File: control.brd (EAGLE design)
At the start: 156 x 38 mm, 68 parts, among them IC3 ATTINY85-20S, U1 L293DD013TR

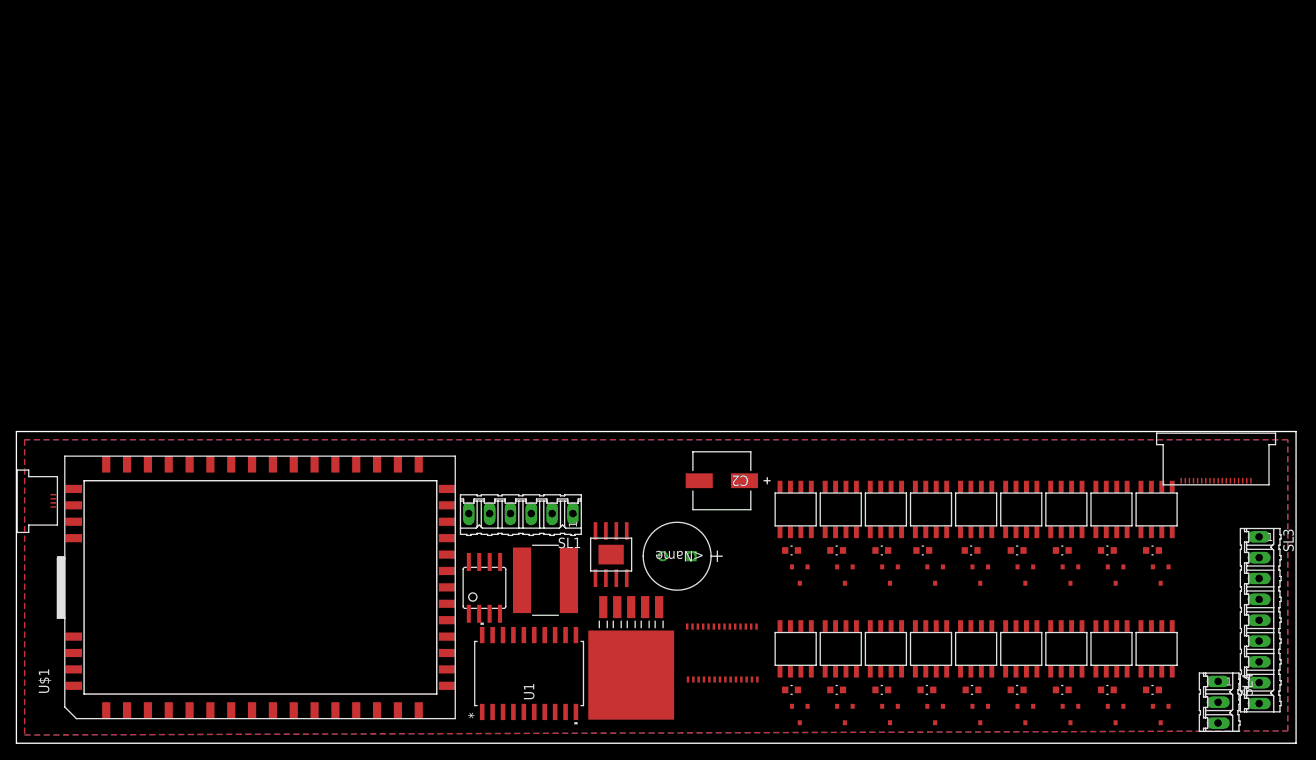
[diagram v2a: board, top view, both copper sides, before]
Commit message: setts up warm cool LED support
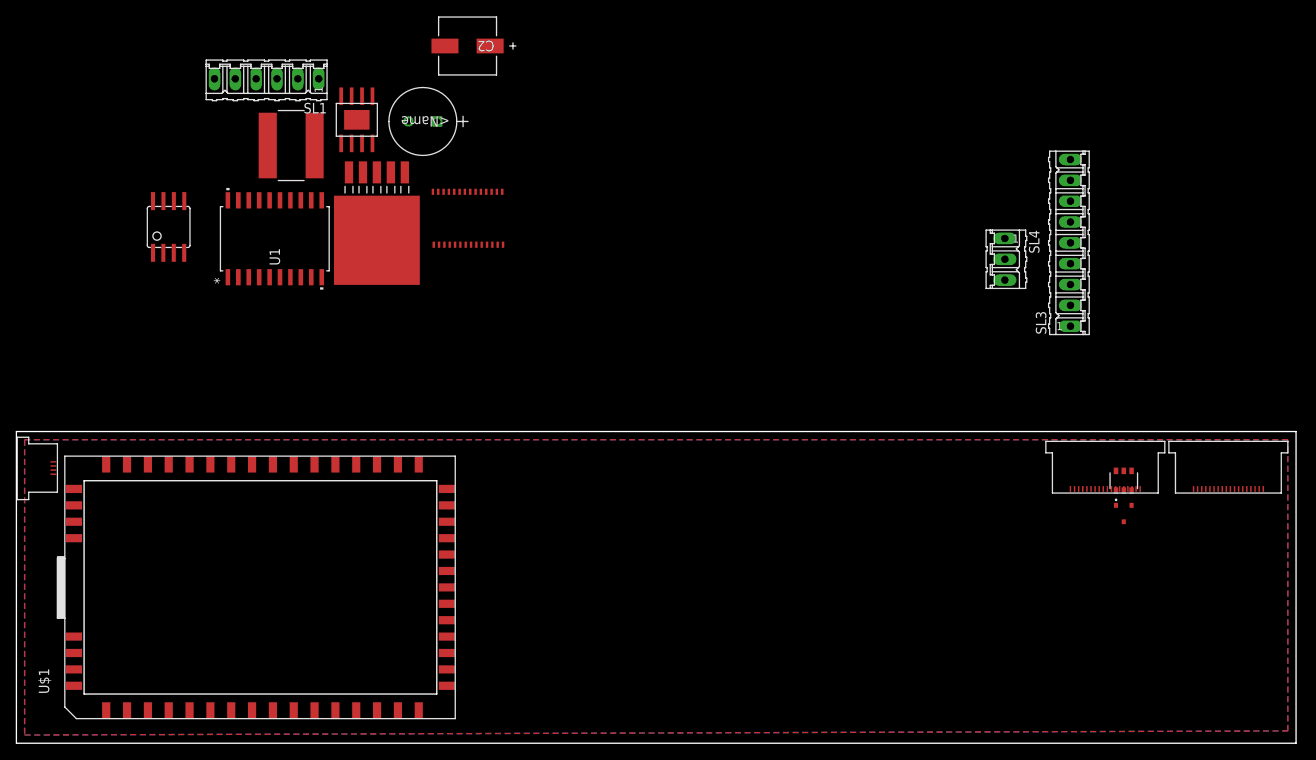
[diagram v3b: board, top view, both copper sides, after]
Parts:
- removed R1, R10, R11, R12, R13, R14, R15, R16, R17, R19, R2, R3, R4, R5, R6, R7, R8, R9: RC0603FR-0710RL, Smile_Shade:RC0603N
- removed U$10, U$12, U$14, U$16, U$18, U$20, U$22, U$24, U$26, U$28, U$30, U$32, U$34, U$4, U$41, U$6, U$8: 2N7002P, Smile_Shade:SOT23
- removed U$11, U$13, U$15, U$17, U$19, U$21, U$23, U$25, U$27, U$29, U$3, U$31, U$33, U$35, U$40, U$5, U$7, U$9: NUD4011DR2G, Smile_Shade:8SOIC
- added U$2: BCR420UW6-7, Smile_Shade:SOT26
- added U$80: SFV18R-3STBE1HLF, Smile_Shade:SFV18R-3STBE1HLF
- moved C2 61.4 mm to (55.0, 85.0)
- moved SL1 61.4 mm to (30.5, 81.0)
- moved U$36 61.4 mm to (33.5, 72.9)
- moved U$37 61.4 mm to (55.0, 64.0)
- moved U$42 61.4 mm to (41.5, 76.0)
- moved U$43 61.4 mm to (43.9, 61.3)
- moved U1 61.4 mm to (31.5, 61.5)
- moved C1 61.4 mm to (47.8, 75.8)
- moved SL4 59.9 mm to (120.5, 59.0)
- moved IC3 58.5 mm to (18.6, 62.9)
- moved SL3 51.4 mm to (128.5, 61.0), turned to 90 degrees
- moved U$38 24.9 mm to (135.0, 28.0)
- moved U$39 4.00 mm to (5.00, 36.5)
- moved U$44 1.80 mm to (152.0, 31.0)
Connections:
- removed net 48: R16.2, U$35.P$1
- removed net N$1: U$3.P$4, U$4.P$3
- removed net N$10: R4.1, U$11.P$3
- removed net N$11: U$12.P$3, U$13.P$4
- removed net N$12: R5.1, U$13.P$3
- removed net N$13: U$10.P$3, U$15.P$4
- removed net N$14: R6.1, U$15.P$3
- removed net N$15: U$17.P$4, U$38.P$3
- removed net N$16: R8.1, U$17.P$3
- removed net N$17: U$18.P$3, U$25.P$4
- removed net N$18: R7.1, U$25.P$3
- removed net N$19: U$20.P$3, U$23.P$4
- removed net N$20: R9.1, U$23.P$3
- removed net N$21: U$21.P$4, U$22.P$3
- removed net N$22: R10.1, U$21.P$3
- removed net N$23: U$19.P$4, U$24.P$3
- removed net N$24: R11.1, U$19.P$3
- removed net N$25: U$27.P$4, U$32.P$3
- removed net N$26: R15.1, U$27.P$3
- removed net N$27: U$29.P$4, U$30.P$3
- removed net N$28: R14.1, U$29.P$3
- removed net N$29: U$28.P$3, U$31.P$4
- removed net N$3: U$5.P$4, U$6.P$3
- removed net N$30: R13.1, U$31.P$3
- removed net N$31: U$26.P$3, U$33.P$4
- removed net N$32: R12.1, U$33.P$3
- removed net N$35: U$34.P$3, U$35.P$4
- removed net N$36: R16.1, U$35.P$3
- removed net N$37: U$40.P$4, U$41.P$3
- removed net N$38: R17.1, U$40.P$3
- removed net N$4: R1.1, U$5.P$3
- removed net N$5: U$7.P$4, U$8.P$3
- removed net N$6: R2.1, U$7.P$3
- removed net N$7: U$16.P$3, U$9.P$4
- removed net N$8: R3.1, U$9.P$3
- removed net N$9: U$11.P$4, U$14.P$3
- removed net ZN16: U$41.P$2
- net 48V: no longer R1.2, R10.2, R11.2, R12.2, R13.2, R14.2, R15.2, R17.2, R19.2, R2.2, R3.2, R4.2, R5.2, R6.2, R7.2, R8.2, R9.2, U$11.P$1, U$13.P$1, U$15.P$1, U$17.P$1, U$19.P$1, U$21.P$1, U$23.P$1, U$25.P$1, U$27.P$1, U$29.P$1, U$3.P$1, U$31.P$1, U$33.P$1, U$40.P$1, U$5.P$1, U$7.P$1, U$9.P$1
- net GND: now also U$2.4; no longer U$10.P$1, U$12.P$1, U$14.P$1, U$16.P$1, U$18.P$1, U$20.P$1, U$22.P$1, U$24.P$1, U$26.P$1, U$28.P$1, U$30.P$1, U$32.P$1, U$34.P$1, U$4.P$1, U$41.P$1, U$6.P$1, U$8.P$1
- net LEDSTR_1: now also U$2.2, U$2.3, U$2.5; no longer U$17.P$5, U$17.P$6, U$17.P$7, U$17.P$8
- net LEDSTR_10: no longer U$23.P$5, U$23.P$6, U$23.P$7, U$23.P$8
- net LEDSTR_11: no longer U$21.P$5, U$21.P$6, U$21.P$7, U$21.P$8
- net LEDSTR_12: no longer U$19.P$5, U$19.P$6, U$19.P$7, U$19.P$8
- net LEDSTR_13: no longer U$27.P$5, U$27.P$6, U$27.P$7, U$27.P$8
- net LEDSTR_14: no longer U$29.P$5, U$29.P$6, U$29.P$7, U$29.P$8
- net LEDSTR_15: no longer U$31.P$5, U$31.P$6, U$31.P$7, U$31.P$8
- net LEDSTR_16: no longer U$33.P$5, U$33.P$6, U$33.P$7, U$33.P$8
- net LEDSTR_17: no longer U$35.P$5, U$35.P$6, U$35.P$7, U$35.P$8
- net LEDSTR_18: no longer U$40.P$5, U$40.P$6, U$40.P$7, U$40.P$8
- net LEDSTR_2: no longer U$3.P$5, U$3.P$6, U$3.P$7, U$3.P$8
- net LEDSTR_3: no longer U$5.P$5, U$5.P$6, U$5.P$7, U$5.P$8
- net LEDSTR_4: no longer U$7.P$5, U$7.P$6, U$7.P$7, U$7.P$8
- net LEDSTR_5: no longer U$9.P$5, U$9.P$6, U$9.P$7, U$9.P$8
- net LEDSTR_6: no longer U$11.P$5, U$11.P$6, U$11.P$7, U$11.P$8
- net LEDSTR_7: no longer U$13.P$5, U$13.P$6, U$13.P$7, U$13.P$8
- net LEDSTR_8: no longer U$15.P$5, U$15.P$6, U$15.P$7, U$15.P$8
- net LEDSTR_9: no longer U$25.P$5, U$25.P$6, U$25.P$7, U$25.P$8
- net N$2: now also U$2.1, U$38.P$3; no longer R19.1, U$3.P$3
- net ZN1: no longer U$4.P$2
- net ZN10: no longer U$30.P$2
- net ZN11: no longer U$32.P$2
- net ZN12: no longer U$24.P$2
- net ZN13: no longer U$18.P$2
- net ZN14: no longer U$20.P$2
- net ZN15: no longer U$22.P$2
- net ZN2: no longer U$6.P$2
- net ZN3: no longer U$8.P$2
- net ZN4: no longer U$12.P$2
- net ZN5: no longer U$14.P$2
- net ZN6: no longer U$16.P$2
- net ZN7: no longer U$10.P$2
- net ZN8: no longer U$26.P$2, U$34.P$2
- net ZN9: no longer U$28.P$2

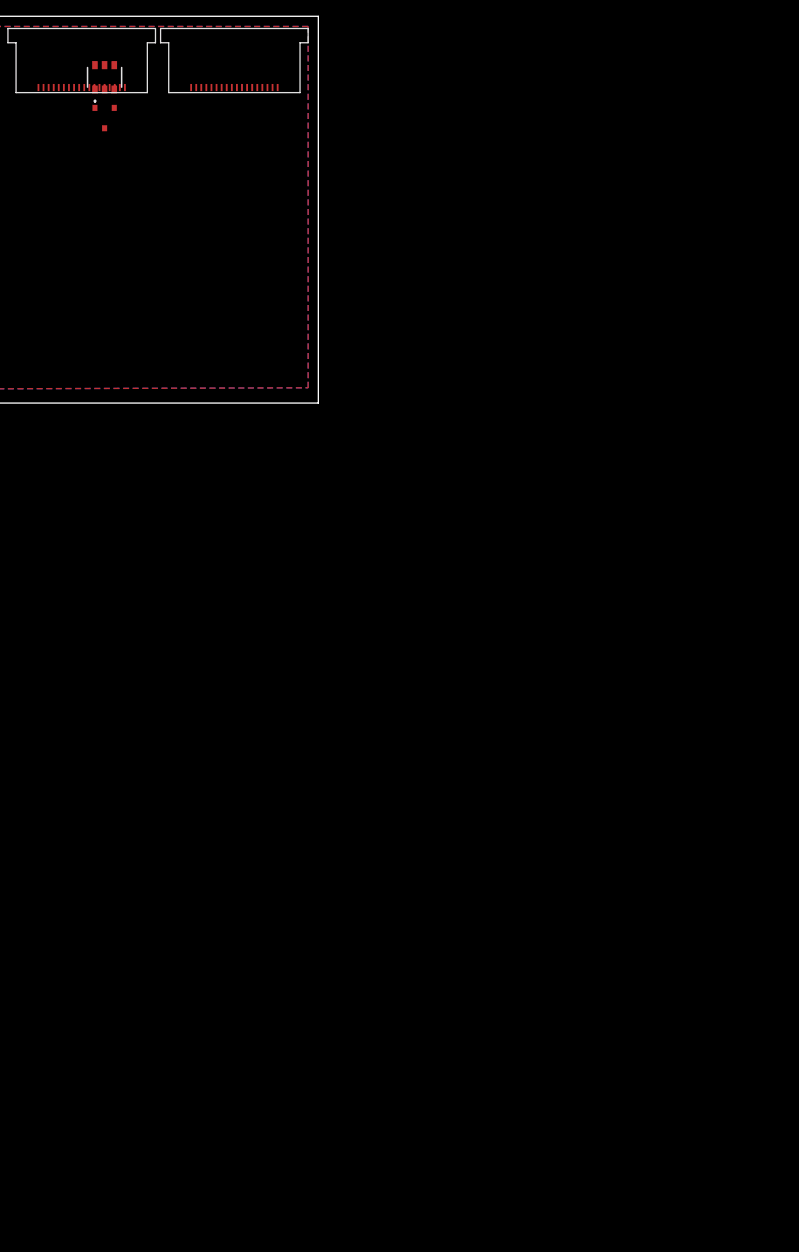
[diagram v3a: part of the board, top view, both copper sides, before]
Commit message: Finalised-ish warm to cool dimming schematic
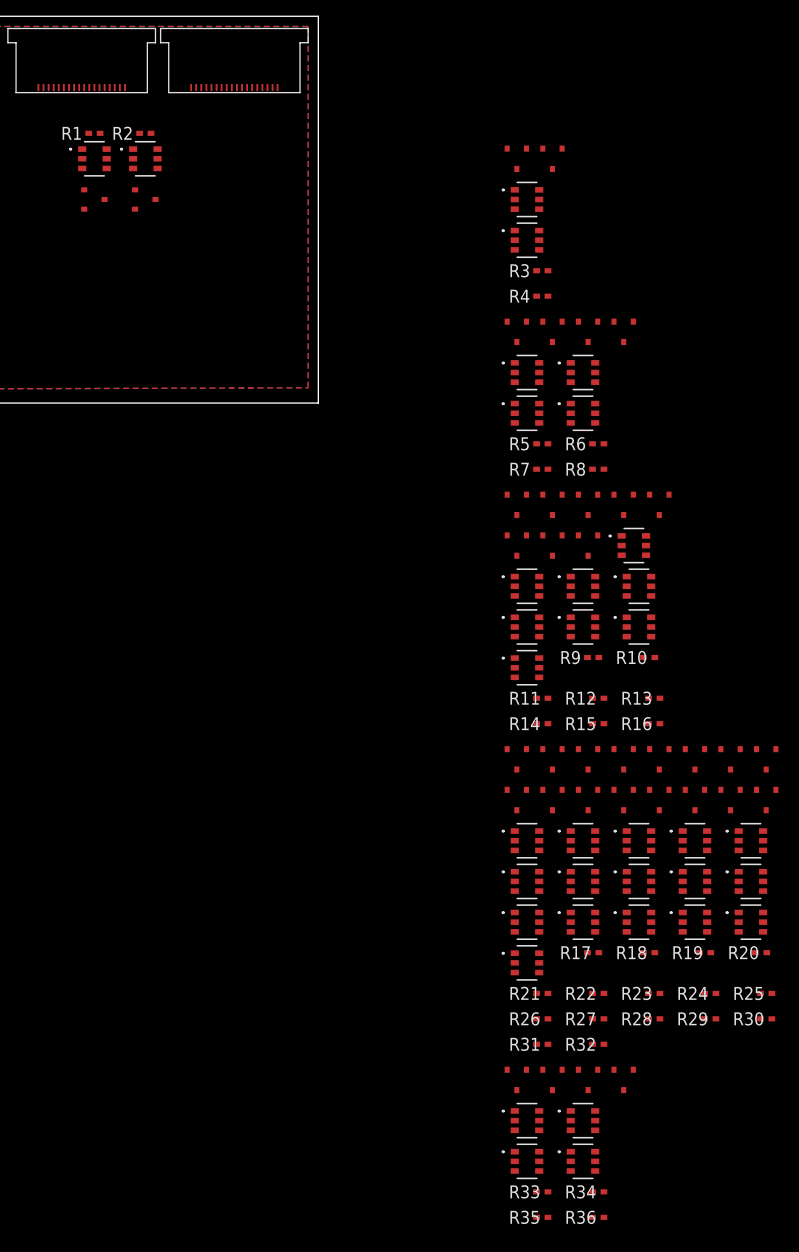
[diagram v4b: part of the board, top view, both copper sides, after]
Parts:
- added R1, R10, R11, R12, R13, R14, R15, R16, R17, R18, R19, R2, R20, R21, R22, R23, R24, R25, R26, R27, R28, R29, R3, R30, R31, R32, R33, R34, R35, R36, R4, R5, R6, R7, R8, R9: RC0402JR-075R1L, Smile_Shade:RC0402N
- added U$10, U$12, U$14, U$16, U$18, U$20, U$22, U$24, U$26, U$28, U$30, U$32, U$34, U$4, U$40, U$45, U$47, U$49, U$51, U$53, U$55, U$57, U$59, U$6, U$61, U$63, U$65, U$67, U$69, U$71, U$73, U$75, U$77, U$79, U$8: BCR420UW6-7, Smile_Shade:SOT26
- added U$11, U$13, U$15, U$17, U$19, U$21, U$23, U$25, U$27, U$29, U$3, U$31, U$33, U$35, U$41, U$46, U$48, U$5, U$50, U$52, U$54, U$56, U$58, U$60, U$62, U$64, U$66, U$68, U$7, U$70, U$72, U$74, U$76, U$78, U$9: 2N7002P, Smile_Shade:SOT23
- moved U$2 8.06 mm to (134.0, 24.0), turned to 0 degrees
- moved U$38 8.06 mm to (134.0, 20.0), turned to 90 degrees
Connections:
- new net GND1: R2.1, U$3.P$1, U$4.4
- new net GND10: R11.1, U$21.P$1, U$22.4
- new net GND11: R12.1, U$23.P$1, U$24.4
- new net GND12: R13.1, U$25.P$1, U$26.4
- new net GND13: R14.1, U$27.P$1, U$28.4
- new net GND14: R15.1, U$29.P$1, U$30.4
- new net GND15: R16.1, U$31.P$1, U$32.4
- new net GND16: R17.1, U$33.P$1, U$34.4
- new net GND17: R18.1, U$35.P$1, U$40.4
- new net GND18: R19.1, U$41.P$1, U$45.4
- new net GND19: R20.1, U$46.P$1, U$47.4
- new net GND2: R3.1, U$5.P$1, U$6.4
- new net GND20: R21.1, U$48.P$1, U$49.4
- new net GND21: R22.1, U$50.P$1, U$51.4
- new net GND22: R23.1, U$52.P$1, U$53.4
- new net GND23: R24.1, U$54.P$1, U$55.4
- new net GND24: R25.1, U$56.P$1, U$57.4
- new net GND25: R26.1, U$58.P$1, U$59.4
- new net GND26: R27.1, U$60.P$1, U$61.4
- new net GND27: R28.1, U$62.P$1, U$63.4
- new net GND28: R29.1, U$64.P$1, U$65.4
- new net GND29: R30.1, U$66.P$1, U$67.4
- new net GND3: R4.1, U$7.P$1, U$8.4
- new net GND30: R31.1, U$68.P$1, U$69.4
- new net GND31: R32.1, U$70.P$1, U$71.4
- new net GND32: R33.1, U$72.P$1, U$73.4
- new net GND33: R34.1, U$74.P$1, U$75.4
- new net GND34: R35.1, U$76.P$1, U$77.4
- new net GND35: R36.1, U$78.P$1, U$79.4
- new net GND4: R5.1, U$10.4, U$9.P$1
- new net GND5: R6.1, U$11.P$1, U$12.4
- new net GND6: R7.1, U$13.P$1, U$14.4
- new net GND7: R8.1, U$15.P$1, U$16.4
- new net GND8: R9.1, U$17.P$1, U$18.4
- new net GND9: R10.1, U$19.P$1, U$20.4
- new net LEDSTR_19: U$10.2, U$10.3, U$10.5
- new net LEDSTR_20: U$12.2, U$12.3, U$12.5
- new net LEDSTR_21: U$14.2, U$14.3, U$14.5
- new net LEDSTR_22: U$16.2, U$16.3, U$16.5
- new net LEDSTR_23: U$18.2, U$18.3, U$18.5
- new net LEDSTR_24: U$20.2, U$20.3, U$20.5
- new net LEDSTR_25: U$22.2, U$22.3, U$22.5
- new net LEDSTR_26: U$24.2, U$24.3, U$24.5
- new net LEDSTR_27: U$26.2, U$26.3, U$26.5
- new net LEDSTR_28: U$28.2, U$28.3, U$28.5
- new net LEDSTR_29: U$30.2, U$30.3, U$30.5
- new net LEDSTR_30: U$32.2, U$32.3, U$32.5
- new net LEDSTR_31: U$34.2, U$34.3, U$34.5
- new net LEDSTR_32: U$40.2, U$40.3, U$40.5
- new net LEDSTR_33: U$45.2, U$45.3, U$45.5
- new net LEDSTR_34: U$47.2, U$47.3, U$47.5
- new net LEDSTR_35: U$49.2, U$49.3, U$49.5
- new net LEDSTR_36: U$51.2, U$51.3, U$51.5
- new net LEDSTR_37: U$53.2, U$53.3, U$53.5
- new net LEDSTR_38: U$55.2, U$55.3, U$55.5
- new net LEDSTR_39: U$57.2, U$57.3, U$57.5
- new net LEDSTR_40: U$59.2, U$59.3, U$59.5
- new net LEDSTR_41: U$61.2, U$61.3, U$61.5
- new net LEDSTR_42: U$63.2, U$63.3, U$63.5
- new net LEDSTR_43: U$65.2, U$65.3, U$65.5
- new net LEDSTR_44: U$67.2, U$67.3, U$67.5
- new net LEDSTR_45: U$69.2, U$69.3, U$69.5
- new net LEDSTR_46: U$71.2, U$71.3, U$71.5
- new net LEDSTR_47: U$73.2, U$73.3, U$73.5
- new net LEDSTR_48: U$75.2, U$75.3, U$75.5
- new net LEDSTR_49: U$77.2, U$77.3, U$77.5
- new net LEDSTR_50: U$79.2, U$79.3, U$79.5
- new net N$1: R1.2, U$2.6
- new net N$10: R5.2, U$10.6
- new net N$11: U$11.P$3, U$12.1
- new net N$12: R6.2, U$12.6
- new net N$13: U$13.P$3, U$14.1
- new net N$14: R7.2, U$14.6
- new net N$15: U$15.P$3, U$16.1
- new net N$16: R8.2, U$16.6
- new net N$17: U$17.P$3, U$18.1
- new net N$18: R9.2, U$18.6
- new net N$19: U$19.P$3, U$20.1
- new net N$20: R10.2, U$20.6
- new net N$21: U$21.P$3, U$22.1
- new net N$22: R11.2, U$22.6
- new net N$23: U$23.P$3, U$24.1
- new net N$24: R12.2, U$24.6
- new net N$25: U$25.P$3, U$26.1
- new net N$26: R13.2, U$26.6
- new net N$27: U$27.P$3, U$28.1
- new net N$28: R14.2, U$28.6
- new net N$29: U$29.P$3, U$30.1
- new net N$3: U$3.P$3, U$4.1
- new net N$30: R15.2, U$30.6
- new net N$31: U$31.P$3, U$32.1
- new net N$32: R16.2, U$32.6
- new net N$35: U$33.P$3, U$34.1
- new net N$36: R17.2, U$34.6
- new net N$37: U$35.P$3, U$40.1
- new net N$38: R18.2, U$40.6
- new net N$4: R2.2, U$4.6
- new net N$42: U$41.P$3, U$45.1
- new net N$43: R19.2, U$45.6
- new net N$44: U$46.P$3, U$47.1
- new net N$45: R20.2, U$47.6
- new net N$46: U$48.P$3, U$49.1
- new net N$47: R21.2, U$49.6
- new net N$48: U$50.P$3, U$51.1
- new net N$49: R22.2, U$51.6
- new net N$5: U$5.P$3, U$6.1
- new net N$50: U$52.P$3, U$53.1
- new net N$51: R23.2, U$53.6
- new net N$52: U$54.P$3, U$55.1
- new net N$53: R24.2, U$55.6
- new net N$54: U$56.P$3, U$57.1
- new net N$55: R25.2, U$57.6
- new net N$56: U$58.P$3, U$59.1
- new net N$57: R26.2, U$59.6
- new net N$58: U$60.P$3, U$61.1
- new net N$59: R27.2, U$61.6
- new net N$6: R3.2, U$6.6
- new net N$60: U$62.P$3, U$63.1
- new net N$61: R28.2, U$63.6
- new net N$62: U$64.P$3, U$65.1
- new net N$63: R29.2, U$65.6
- new net N$64: U$66.P$3, U$67.1
- new net N$65: R30.2, U$67.6
- new net N$66: U$68.P$3, U$69.1
- new net N$67: R31.2, U$69.6
- new net N$68: U$70.P$3, U$71.1
- new net N$69: R32.2, U$71.6
- new net N$7: U$7.P$3, U$8.1
- new net N$70: U$72.P$3, U$73.1
- new net N$71: R33.2, U$73.6
- new net N$72: U$74.P$3, U$75.1
- new net N$73: R34.2, U$75.6
- new net N$74: U$76.P$3, U$77.1
- new net N$75: R35.2, U$77.6
- new net N$76: U$78.P$3, U$79.1
- new net N$77: R36.2, U$79.6
- new net N$8: R4.2, U$8.6
- new net N$9: U$10.1, U$9.P$3
- new net ZN16: U$3.P$2
- new net ZN17: U$5.P$2
- new net ZN18: U$7.P$2
- new net ZN19: U$9.P$2
- new net ZN20: U$11.P$2
- new net ZN21: U$13.P$2
- new net ZN22: U$15.P$2
- new net ZN23: U$17.P$2
- new net ZN24: U$19.P$2
- new net ZN25: U$21.P$2
- new net ZN26: U$23.P$2
- new net ZN27: U$25.P$2
- new net ZN28: U$27.P$2
- new net ZN29: U$29.P$2
- new net ZN30: U$31.P$2
- new net ZN31: U$33.P$2
- new net ZN32: U$35.P$2
- new net ZN33: U$41.P$2
- new net ZN34: U$46.P$2
- new net ZN35: U$48.P$2
- new net ZN36: U$50.P$2
- new net ZN37: U$52.P$2
- new net ZN38: U$54.P$2
- new net ZN39: U$56.P$2
- new net ZN40: U$58.P$2
- new net ZN41: U$60.P$2
- new net ZN42: U$62.P$2
- new net ZN43: U$64.P$2
- new net ZN44: U$66.P$2
- new net ZN45: U$68.P$2
- new net ZN46: U$70.P$2
- new net ZN47: U$72.P$2
- new net ZN48: U$74.P$2
- new net ZN49: U$76.P$2
- new net ZN50: U$78.P$2
- net GND: now also R1.1
- net LEDSTR_2: now also U$4.2, U$4.3, U$4.5
- net LEDSTR_3: now also U$6.2, U$6.3, U$6.5
- net LEDSTR_4: now also U$8.2, U$8.3, U$8.5
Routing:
- added copper zone on layer 1, net GND
- removed copper zone on layer 1, net GNDDD
